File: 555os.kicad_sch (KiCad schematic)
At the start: 4 parts, among them U1 XL1509-12

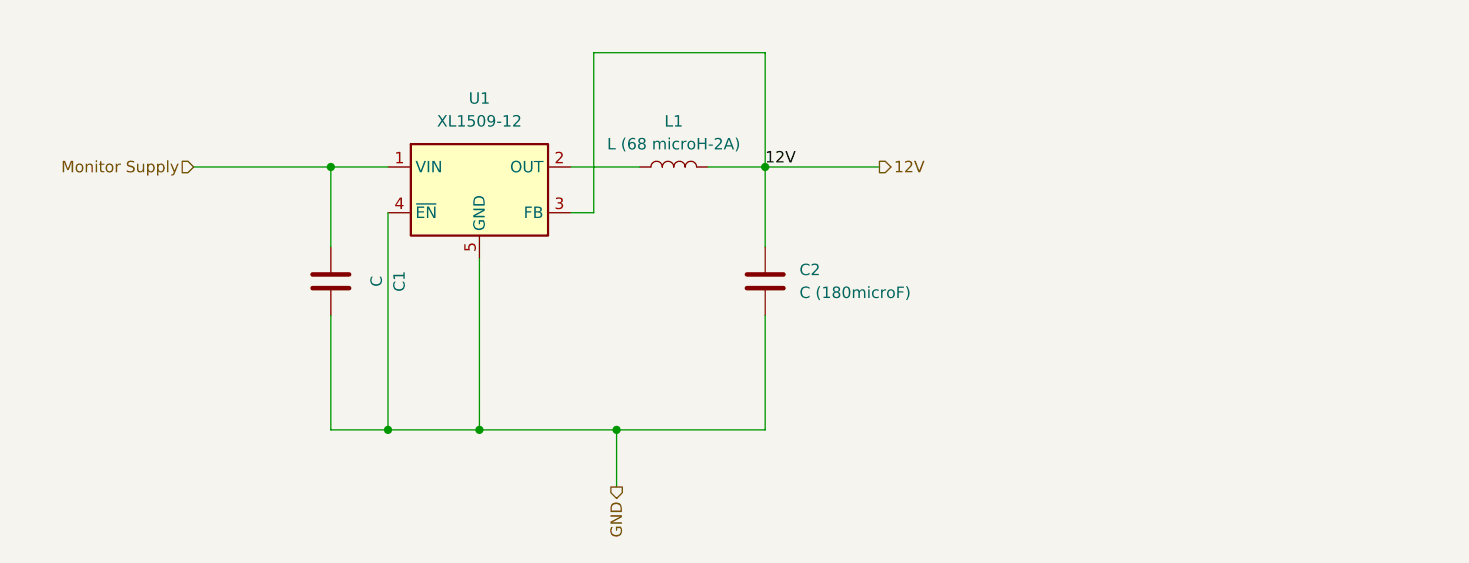
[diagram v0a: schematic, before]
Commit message: Big? Update
Turned back to Bilateral Hall Sensor, added Analog Voltage Multiplier.
Added 555 oneshot timer for closing relay on boot.
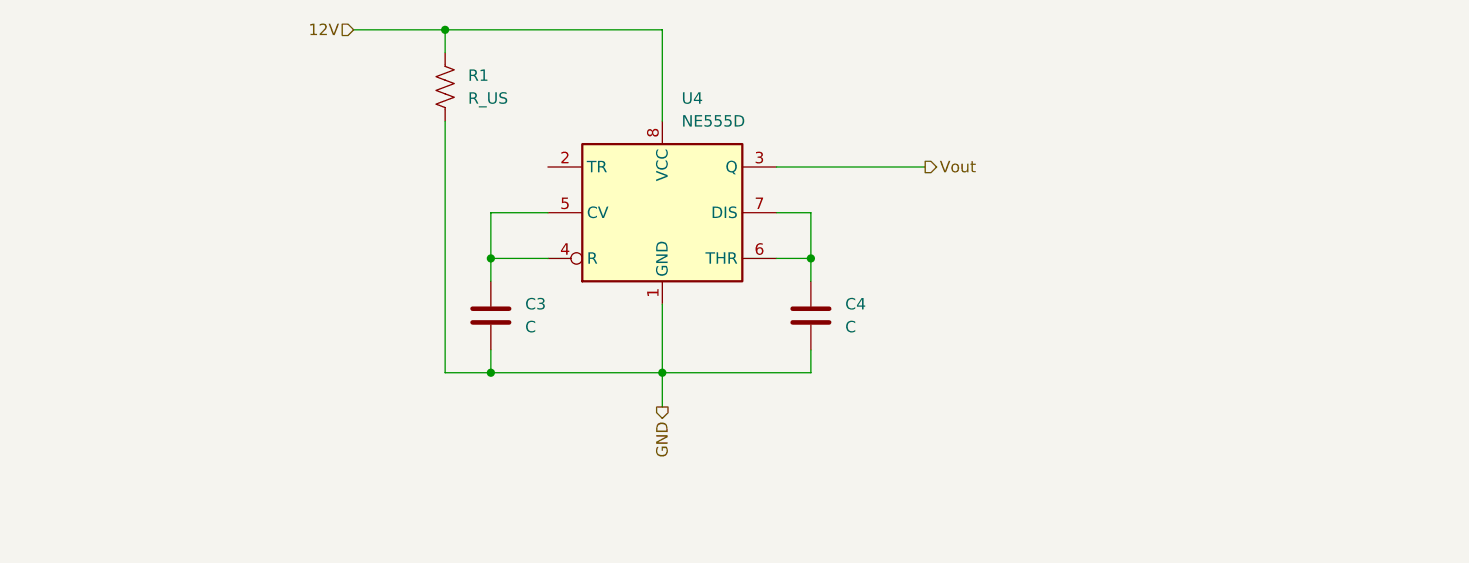
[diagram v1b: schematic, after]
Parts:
- removed C1: C, symbol Device:C
- removed C2: C (180microF), symbol Device:C
- removed L1: L (68 microH-2A), symbol Device:L
- removed U1: XL1509-12, Package_SO:SOIC-8_3.9x4.9mm_P1.27mm, symbol Regulator_Switching:XL1509-12
- added C3, C4: C, symbol Device:C
- added R1: R_US, symbol Device:R_US
- added U4: NE555D, Package_SO:SOIC-8_3.9x4.9mm_P1.27mm, symbol Timer:NE555D
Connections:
- net 12V: now also R1.1, U4.8 (VCC)
- net GND: now also C3.1, C4.1, R1.2, U4.1 (GND)
- new net: C3.2, U4.4 (R), U4.5 (CV)
- new net: C4.2, U4.6 (THR), U4.7 (DIS)
- new net Vout: U4.3 (Q)

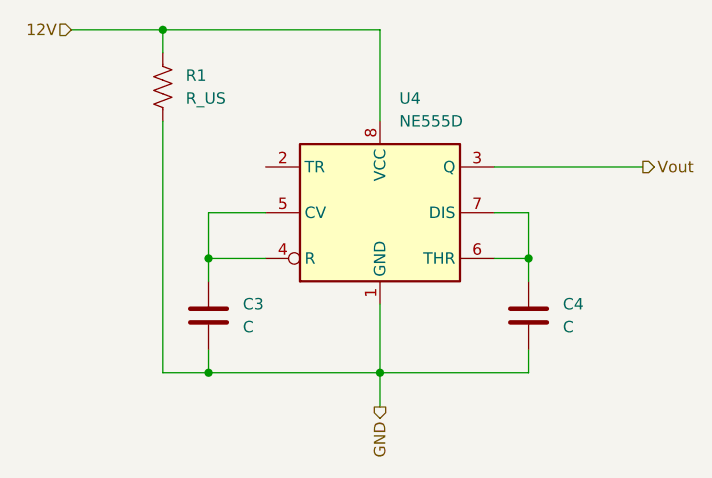
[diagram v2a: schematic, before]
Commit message: Ri-organization
Put circuit in better order
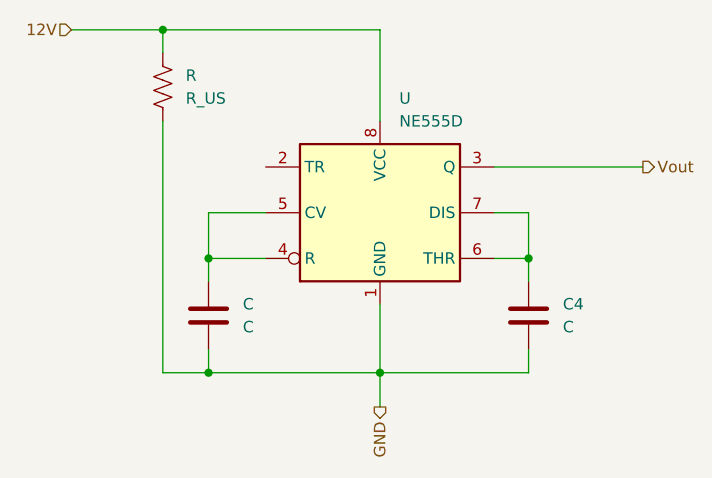
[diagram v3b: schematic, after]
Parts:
- renumbered C3 to C, R1 to R, U4 to U
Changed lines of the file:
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@@
 		(dnp no)
 		(fields_autoplaced yes)
-		(property "Reference" "U4"
+		(property "Reference" "U"
 			(at 150.7333 71.12 0)
 			(effects
@@
 		)
 		(instances
-			(project ""
-				(path "/bdc7face-9f7c-4701-80bb-4cc144448db1/99c0648b-9ff3-4ff9-be70-cb74ae70b46a"
-					(reference "U4")
+			(project "recruitment"
+				(path "/bdc7face-9f7c-4701-80bb-4cc144448db1/daa37310-17dc-447e-86b6-d7c579994776"
+					(reference "U5")
 					(unit 1)
 				)
@@
 		(dnp no)
 		(fields_autoplaced yes)
-		(property "Reference" "C3"
+		(property "Reference" "C"
 			(at 133.35 93.9799 0)
 			(effects
@@
 		)
 		(instances
-			(project ""
-				(path "/bdc7face-9f7c-4701-80bb-4cc144448db1/99c0648b-9ff3-4ff9-be70-cb74ae70b46a"
-					(reference "C3")
+			(project "recruitment"
+				(path "/bdc7face-9f7c-4701-80bb-4cc144448db1/daa37310-17dc-447e-86b6-d7c579994776"
+					(reference "C5")
 					(unit 1)
 				)
@@
 		(dnp no)
 		(fields_autoplaced yes)
-		(property "Reference" "R1"
+		(property "Reference" "R"
 			(at 127 68.5799 0)
 			(effects
@@
 		)
 		(instances
-			(project ""
-				(path "/bdc7face-9f7c-4701-80bb-4cc144448db1/99c0648b-9ff3-4ff9-be70-cb74ae70b46a"
-					(reference "R1")
+			(project "recruitment"
+				(path "/bdc7face-9f7c-4701-80bb-4cc144448db1/daa37310-17dc-447e-86b6-d7c579994776"
+					(reference "R4")
 					(unit 1)
 				)
@@
 					(unit 1)
 				)
+				(path "/bdc7face-9f7c-4701-80bb-4cc144448db1/daa37310-17dc-447e-86b6-d7c579994776"
+					(reference "C6")
+					(unit 1)
+				)

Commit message: Temp Update
Added comments, Op Amp, changed tags, added some wiring, prepared for finalization of Schematic.
(Still missing some values)
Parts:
- renumbered C to C?, R to R?, U to U?
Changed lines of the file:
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@@
 		(dnp no)
 		(fields_autoplaced yes)
-		(property "Reference" "U"
+		(property "Reference" "U?"
 			(at 150.7333 71.12 0)
 			(effects
@@
 		(instances
 			(project "recruitment"
+				(path "/bdc7face-9f7c-4701-80bb-4cc144448db1/99c0648b-9ff3-4ff9-be70-cb74ae70b46a"
+					(reference "U?")
+					(unit 1)
+				)
 				(path "/bdc7face-9f7c-4701-80bb-4cc144448db1/daa37310-17dc-447e-86b6-d7c579994776"
 					(reference "U5")
@@
 		(dnp no)
 		(fields_autoplaced yes)
-		(property "Reference" "C"
+		(property "Reference" "C?"
 			(at 133.35 93.9799 0)
 			(effects
@@
 		(instances
 			(project "recruitment"
+				(path "/bdc7face-9f7c-4701-80bb-4cc144448db1/99c0648b-9ff3-4ff9-be70-cb74ae70b46a"
+					(reference "C?")
+					(unit 1)
+				)
 				(path "/bdc7face-9f7c-4701-80bb-4cc144448db1/daa37310-17dc-447e-86b6-d7c579994776"
 					(reference "C5")
@@
 		(dnp no)
 		(fields_autoplaced yes)
-		(property "Reference" "R"
+		(property "Reference" "R?"
 			(at 127 68.5799 0)
 			(effects
@@
 		(instances
 			(project "recruitment"
+				(path "/bdc7face-9f7c-4701-80bb-4cc144448db1/99c0648b-9ff3-4ff9-be70-cb74ae70b46a"
+					(reference "R?")
+					(unit 1)
+				)
 				(path "/bdc7face-9f7c-4701-80bb-4cc144448db1/daa37310-17dc-447e-86b6-d7c579994776"
 					(reference "R4")

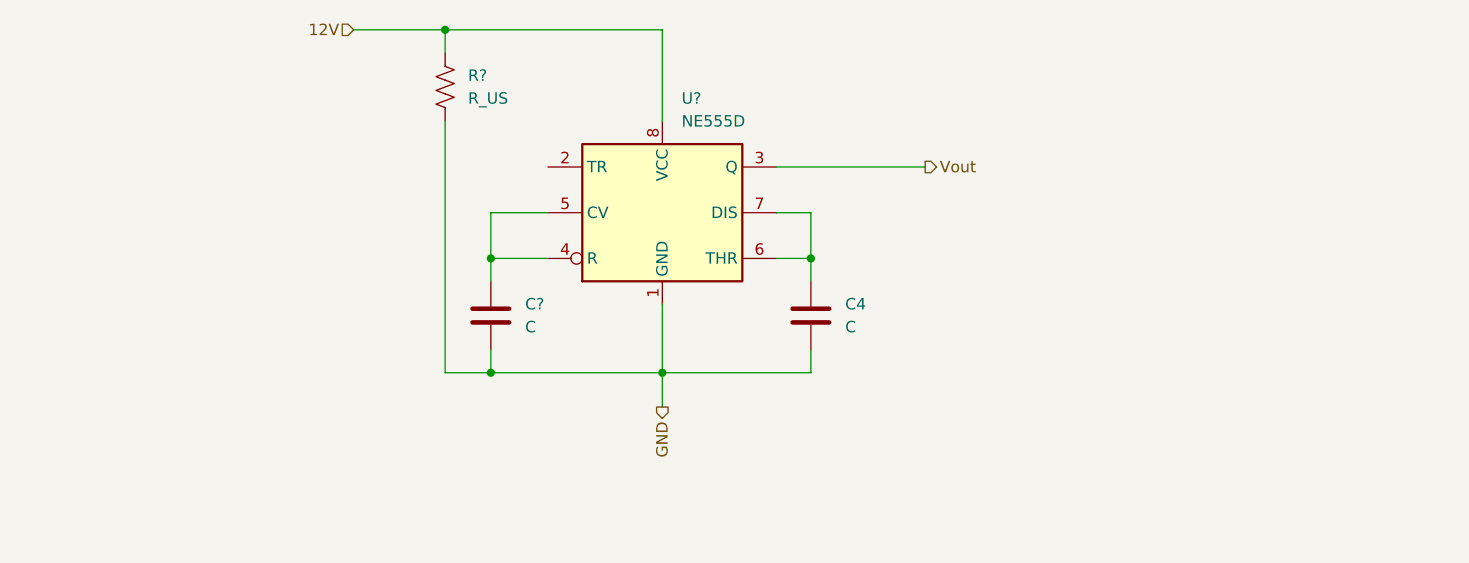
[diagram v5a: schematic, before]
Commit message: Schematic Complete
Completed the wiring of the circuit.

(Missing some labels and footprints)
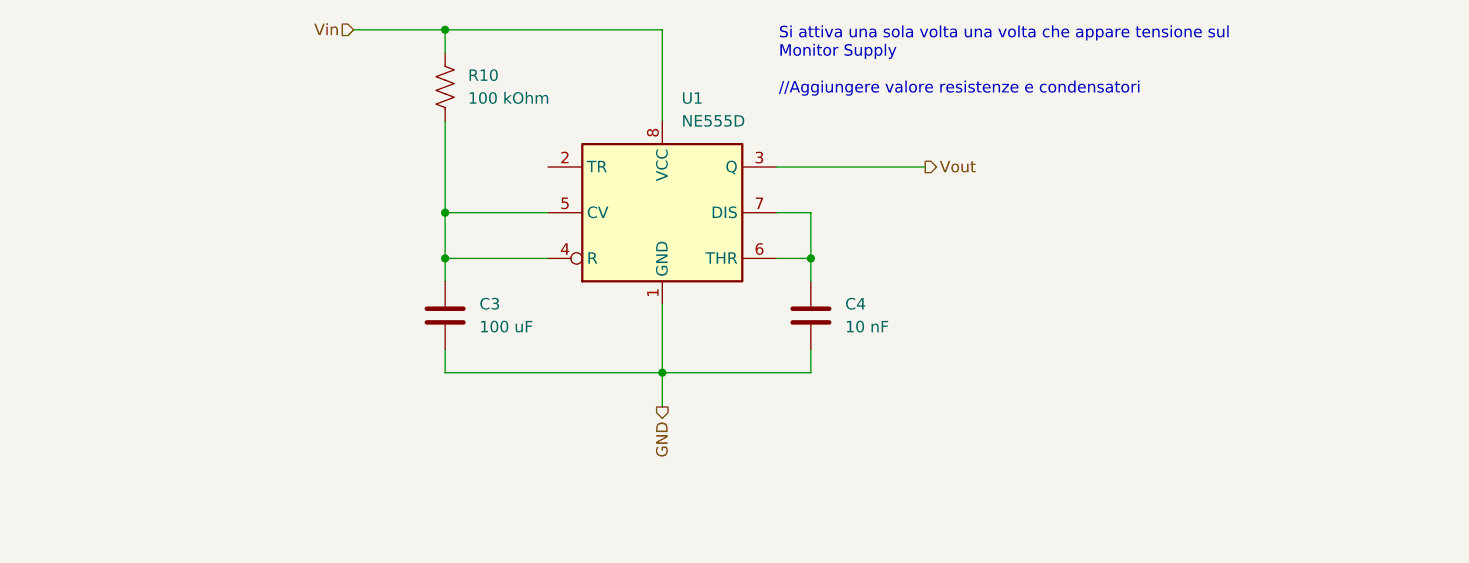
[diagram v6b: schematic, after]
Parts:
- C3: renamed from C?; value C -> 100 uF; footprint (none) -> Capacitor_THT:C_Radial_D8.0mm_H7.0mm_P3.50mm
- C4: value C -> 10 nF
- R10: renamed from R?; value R_US -> 100 kOhm
- gave numbers to parts that had none: 1
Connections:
- net GND: no longer R10.2
- net at C3.2, U1.4 (R), U1.5 (CV): now also R10.2
- net 12V renamed Vin
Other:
- note added: "Si attiva una sola volta una volta che appare tensione sul Monitor Supply //Aggiungere valore resistenze e condensatori"
- moved on the sheet: C3
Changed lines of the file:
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@@
 	(generator_version "9.0")
 	(paper "A4")
+	(text "Si attiva una sola volta una volta che appare tensione sul\nMonitor Supply\n\n//Aggiungere valore resistenze e condensatori"
+		(exclude_from_sim no)
+		(at 161.544 67.056 0)
+		(effects
+			(font
+				(size 1.27 1.27)
+			)
+			(justify left)
+		)
+	)
 	(junction
-		(at 129.54 101.6)
-		(diameter 0)
-		(color 0 0 0 0)
-	)
-	(junction
-		(at 129.54 88.9)
+		(at 124.46 88.9)
 		(diameter 0)
 		(color 0 0 0 0)
@@
 		(color 0 0 0 0)
 	)
+	(junction
+		(at 124.46 83.82)
+		(diameter 0)
+		(color 0 0 0 0)
+	)
 	(wire
 		(pts
@@
 	(wire
 		(pts
-			(xy 129.54 88.9) (xy 129.54 91.44)
+			(xy 124.46 88.9) (xy 124.46 91.44)
 		)
 		(stroke
@@
 	(wire
 		(pts
-			(xy 124.46 101.6) (xy 129.54 101.6)
-		)
-		(stroke
-			(width 0)
-			(type default)
-		)
-	)
-	(wire
-		(pts
-			(xy 129.54 99.06) (xy 129.54 101.6)
+			(xy 124.46 99.06) (xy 124.46 101.6)
 		)
 		(stroke
@@
 	(wire
 		(pts
-			(xy 129.54 83.82) (xy 129.54 88.9)
-		)
-		(stroke
-			(width 0)
-			(type default)
-		)
-	)
-	(wire
-		(pts
 			(xy 165.1 99.06) (xy 165.1 101.6)
 		)
@@
 	(wire
 		(pts
+			(xy 124.46 101.6) (xy 148.59 101.6)
+		)
+		(stroke
+			(width 0)
+			(type default)
+		)
+	)
+	(wire
+		(pts
 			(xy 161.29 88.9) (xy 165.1 88.9)
 		)
@@
 	(wire
 		(pts
+			(xy 124.46 83.82) (xy 124.46 88.9)
+		)
+		(stroke
+			(width 0)
+			(type default)
+		)
+	)
+	(wire
+		(pts
 			(xy 124.46 63.5) (xy 148.59 63.5)
 		)
@@
 	(wire
 		(pts
-			(xy 124.46 73.66) (xy 124.46 101.6)
-		)
-		(stroke
-			(width 0)
-			(type default)
-		)
-	)
-	(wire
-		(pts
-			(xy 129.54 88.9) (xy 135.89 88.9)
-		)
-		(stroke
-			(width 0)
-			(type default)
-		)
-	)
-	(wire
-		(pts
-			(xy 129.54 101.6) (xy 148.59 101.6)
-		)
-		(stroke
-			(width 0)
-			(type default)
-		)
-	)
-	(wire
-		(pts
-			(xy 135.89 83.82) (xy 129.54 83.82)
+			(xy 124.46 73.66) (xy 124.46 83.82)
+		)
+		(stroke
+			(width 0)
+			(type default)
+		)
+	)
+	(wire
+		(pts
+			(xy 124.46 88.9) (xy 135.89 88.9)
+		)
+		(stroke
+			(width 0)
+			(type default)
+		)
+	)
+	(wire
+		(pts
+			(xy 135.89 83.82) (xy 124.46 83.82)
 		)
 		(stroke
@@
 		)
 	)
-	(hierarchical_label "12V"
-		(shape input)
-		(at 114.3 63.5 180)
+	(hierarchical_label "GND"
+		(shape output)
+		(at 148.59 105.41 270)
 		(effects
 			(font
@@
 		)
 	)
-	(hierarchical_label "GND"
-		(shape output)
-		(at 148.59 105.41 270)
+	(hierarchical_label "Vin"
+		(shape input)
+		(at 114.3 63.5 180)
 		(effects
 			(font
@@
 		(dnp no)
 		(fields_autoplaced yes)
-		(property "Reference" "U?"
+		(property "Reference" "U1"
 			(at 150.7333 71.12 0)
 			(effects
@@
 			(project "recruitment"
 				(path "/bdc7face-9f7c-4701-80bb-4cc144448db1/99c0648b-9ff3-4ff9-be70-cb74ae70b46a"
-					(reference "U?")
+					(reference "U1")
 					(unit 1)
 				)
@@
 	(symbol
 		(lib_id "Device:C")
-		(at 129.54 95.25 180)
+		(at 124.46 95.25 180)
 		(unit 1)
 		(exclude_from_sim no)
@@
 		(dnp no)
 		(fields_autoplaced yes)
-		(property "Reference" "C?"
-			(at 133.35 93.9799 0)
+		(property "Reference" "C3"
+			(at 128.27 93.9799 0)
 			(effects
 				(font
@@
 			)
 		)
-		(property "Value" "C"
-			(at 133.35 96.5199 0)
+		(property "Value" "100 uF"
+			(at 128.27 96.5199 0)
 			(effects
 				(font
@@
 			)
 		)
-		(property "Footprint" ""
-			(at 128.5748 91.44 0)
+		(property "Footprint" "Capacitor_THT:C_Radial_D8.0mm_H7.0mm_P3.50mm"
+			(at 123.4948 91.44 0)
 			(effects
 				(font
@@
 		)
 		(property "Datasheet" "~"
-			(at 129.54 95.25 0)
+			(at 124.46 95.25 0)
 			(effects
 				(font
@@
 		)
 		(property "Description" "Unpolarized capacitor"
-			(at 129.54 95.25 0)
+			(at 124.46 95.25 0)
 			(effects
 				(font
@@
 			(project "recruitment"
 				(path "/bdc7face-9f7c-4701-80bb-4cc144448db1/99c0648b-9ff3-4ff9-be70-cb74ae70b46a"
-					(reference "C?")
+					(reference "C3")
 					(unit 1)
 				)
@@
 		(dnp no)
 		(fields_autoplaced yes)
-		(property "Reference" "R?"
+		(property "Reference" "R10"
 			(at 127 68.5799 0)
 			(effects
@@
 			)
 		)
-		(property "Value" "R_US"
+		(property "Value" "100 kOhm"
 			(at 127 71.1199 0)
 			(effects
@@
 			(project "recruitment"
 				(path "/bdc7face-9f7c-4701-80bb-4cc144448db1/99c0648b-9ff3-4ff9-be70-cb74ae70b46a"
-					(reference "R?")
+					(reference "R10")
 					(unit 1)
 				)
@@
 			)
 		)
-		(property "Value" "C"
+		(property "Value" "10 nF"
 			(at 168.91 96.5199 0)
 			(effects

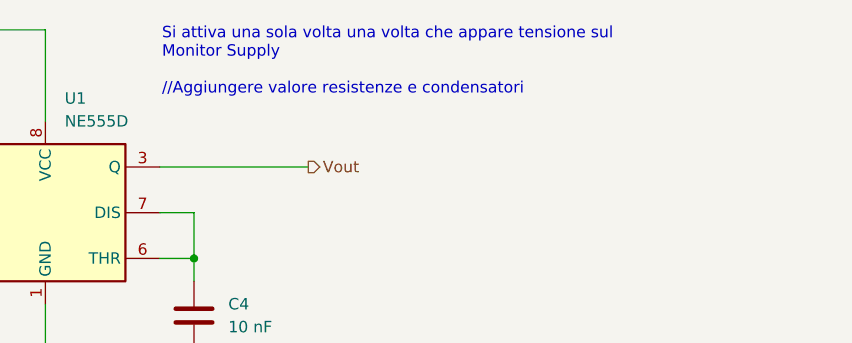
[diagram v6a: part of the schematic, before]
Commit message: Finished (?)
Assigned al values, footprints and generated traces.
Generated DRL files.
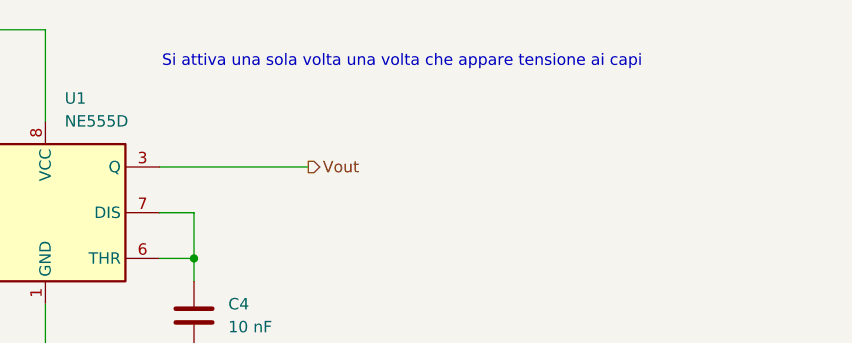
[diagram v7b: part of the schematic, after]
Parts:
- C4: footprint (none) -> Capacitor_SMD:C_0402_1005Metric
- R10: footprint (none) -> Resistor_SMD:R_1206_3216Metric_Pad1.30x1.75mm_HandSolder
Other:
- note added: "Si attiva una sola volta una volta che appare tensione ai capi"
- note removed: "Si attiva una sola volta una volta che appare tensione sul Monitor Supply //Aggiungere valore resistenze e condensatori"
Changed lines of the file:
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@@
 	(generator_version "9.0")
 	(paper "A4")
-	(text "Si attiva una sola volta una volta che appare tensione sul\nMonitor Supply\n\n//Aggiungere valore resistenze e condensatori"
+	(text "Si attiva una sola volta una volta che appare tensione ai capi"
 		(exclude_from_sim no)
 		(at 161.544 67.056 0)
@@
 			)
 		)
-		(property "Footprint" ""
+		(property "Footprint" "Resistor_SMD:R_1206_3216Metric_Pad1.30x1.75mm_HandSolder"
 			(at 125.476 70.104 90)
 			(effects
@@
 			)
 		)
-		(property "Footprint" ""
+		(property "Footprint" "Capacitor_SMD:C_0402_1005Metric"
 			(at 164.1348 91.44 0)
 			(effects
